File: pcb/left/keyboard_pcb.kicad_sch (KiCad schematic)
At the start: 44 parts, among them J1 TRRS, J2 Conn_01x04_Male, K0 KEYSW, K1 KEYSW, K10 KEYSW, K11 KEYSW, K12 KEYSW, K13 KEYSW, K14 KEYSW, K15 KEYSW, K2 KEYSW, K20 KEYSW, K21 KEYSW, K22 KEYSW, K23 KEYSW, K24 KEYSW, K25 KEYSW, K3 KEYSW, K30 KEYSW, K31 KEYSW, K32 KEYSW, K4 KEYSW, K5 KEYSW, U1 PCF8574, U2 Pico

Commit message: first layout left
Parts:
- C1: value C -> 10uF
- C2: value C -> 100nF
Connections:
- net I2C_Int: now also U2.22 (GPIO17); no longer U2.27 (GPIO21)
- net k00: now also U1.6 (P2); no longer U1.4 (P0)
- net k01: now also U2.15 (GPIO11); no longer U2.29 (GPIO22)
- net k03: now also U2.6 (GPIO4); no longer U2.20 (GPIO15)
- net k11: now also U2.14 (GPIO10); no longer U2.26 (GPIO20)
- net k12: now also U2.12 (GPIO9); no longer U2.24 (GPIO18)
- net k13: now also U2.11 (GPIO8); no longer U2.19 (GPIO14)
- net k14: now also U2.10 (GPIO7); no longer U2.22 (GPIO17)
- net k15: now also U2.9 (GPIO6); no longer U2.21 (GPIO16)
- net k20: now also U1.4 (P0); no longer U1.6 (P2)
- net k21: now also U2.21 (GPIO16); no longer U2.25 (GPIO19)
- net k22: now also U2.19 (GPIO14); no longer U2.9 (GPIO6)
- net k23: now also U2.16 (GPIO12); no longer U2.10 (GPIO7)
- net k24: now also U2.20 (GPIO15); no longer U2.17 (GPIO13)
- net k25: now also U2.17 (GPIO13); no longer U2.6 (GPIO4)
- no-connect marks 12 -> 11
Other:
- moved on the sheet: C1, C2, R3, R4

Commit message: Added changes on the left board
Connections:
- net SCL: no longer U2.32 (GPIO27_ADC1)
- net SDA: no longer U2.31 (GPIO26_ADC0)
- net k01: now also U2.24 (GPIO18); no longer U2.15 (GPIO11)
- net k11: now also U2.25 (GPIO19); no longer U2.14 (GPIO10)
- net k12: now also U2.32 (GPIO27_ADC1); no longer U2.12 (GPIO9)
- net k13: now also U2.31 (GPIO26_ADC0); no longer U2.11 (GPIO8)
- net k23: now also U2.26 (GPIO20); no longer U2.16 (GPIO12)
- no-connect marks 11 -> 13
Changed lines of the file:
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@@
   (junction (at 193.04 142.24) (diameter 0) (color 0 0 0 0)
   )
-  (no_connect (at 68.58 67.31))
   (no_connect (at 68.58 57.15))
-  (no_connect (at 68.58 64.77))
+  (no_connect (at 27.94 64.77))
+  (no_connect (at 27.94 54.61))
+  (no_connect (at 27.94 62.23))
+  (no_connect (at 27.94 57.15))
   (no_connect (at 53.34 82.55))
   (no_connect (at 50.8 82.55))
   (no_connect (at 48.26 82.55))
+  (no_connect (at 27.94 67.31))
   (no_connect (at 68.58 39.37))
   (no_connect (at 68.58 41.91))
   (no_connect (at 68.58 36.83))
   (no_connect (at 68.58 54.61))
-  (no_connect (at 68.58 69.85))
   (wire (pts (xy 149.86 60.96) (xy 154.94 60.96))
     (stroke (width 0) (type default) (color 0 0 0 0))
@@
     (stroke (width 0) (type default) (color 0 0 0 0))
   )
+  (polyline (pts (xy 26.67 53.34) (xy 29.21 53.34))
+    (stroke (width 0) (type default) (color 0 0 0 0))
+  )
   (wire (pts (xy 193.04 139.7) (xy 201.93 139.7))
     (stroke (width 0) (type default) (color 0 0 0 0))
@@
     (stroke (width 0) (type default) (color 0 0 0 0))
   )
+  (polyline (pts (xy 26.67 53.34) (xy 22.86 53.34))
+    (stroke (width 0) (type default) (color 0 0 0 0))
+  )
   (wire (pts (xy 248.92 124.46) (xy 248.92 120.65))
     (stroke (width 0) (type default) (color 0 0 0 0))
   )
-  (wire (pts (xy 27.94 69.85) (xy 33.02 69.85))
-    (stroke (width 0) (type default) (color 0 0 0 0))
-  )
-  (wire (pts (xy 68.58 77.47) (xy 85.09 77.47))
+  (wire (pts (xy 21.59 69.85) (xy 33.02 69.85))
     (stroke (width 0) (type default) (color 0 0 0 0))
   )
@@
     (stroke (width 0) (type default) (color 0 0 0 0))
   )
+  (polyline (pts (xy 22.86 68.58) (xy 30.48 68.58))
+    (stroke (width 0) (type default) (color 0 0 0 0))
+  )
   (wire (pts (xy 227.33 139.7) (xy 231.14 139.7))
     (stroke (width 0) (type default) (color 0 0 0 0))
@@
     (stroke (width 0) (type default) (color 0 0 0 0))
   )
+  (polyline (pts (xy 22.86 53.34) (xy 22.86 68.58))
+    (stroke (width 0) (type default) (color 0 0 0 0))
+  )
   (wire (pts (xy 271.78 78.74) (xy 271.78 76.2))
     (stroke (width 0) (type default) (color 0 0 0 0))
@@
     (stroke (width 0) (type default) (color 0 0 0 0))
   )
-  (label "k11" (at 27.94 62.23 180)
-    (effects (font (size 1.27 1.27)) (justify right bottom))
+  (label "k11" (at 68.58 67.31 0)
+    (effects (font (size 1.27 1.27)) (justify left bottom))
   )
   (label "SCL" (at 148.59 151.13 180)
@@
     (effects (font (size 1.27 1.27)) (justify left bottom))
   )
-  (label "k21" (at 85.09 77.47 0)
-    (effects (font (size 1.27 1.27)) (justify left bottom))
-  )
-  (label "k13" (at 27.94 54.61 180)
-    (effects (font (size 1.27 1.27)) (justify right bottom))
+  (label "k21" (at 68.58 77.47 0)
+    (effects (font (size 1.27 1.27)) (justify left bottom))
+  )
+  (label "k13" (at 77.47 52.07 0)
+    (effects (font (size 1.27 1.27)) (justify left bottom))
   )
   (label "k30" (at 200.66 76.2 0)
@@
     (effects (font (size 1.27 1.27)) (justify left bottom))
   )
-  (label "SDA" (at 77.47 52.07 180)
+  (label "SDA" (at 19.05 62.23 180)
     (effects (font (size 1.27 1.27)) (justify right bottom))
   )
@@
     (effects (font (size 1.27 1.27)) (justify left bottom))
   )
-  (label "k01" (at 27.94 64.77 180)
-    (effects (font (size 1.27 1.27)) (justify right bottom))
+  (label "k01" (at 68.58 69.85 0)
+    (effects (font (size 1.27 1.27)) (justify left bottom))
   )
   (label "k00" (at 124.46 30.48 0)
@@
     (effects (font (size 1.27 1.27)) (justify left bottom))
   )
-  (label "k12" (at 27.94 57.15 180)
-    (effects (font (size 1.27 1.27)) (justify right bottom))
+  (label "k12" (at 77.47 49.53 0)
+    (effects (font (size 1.27 1.27)) (justify left bottom))
   )
   (label "k30" (at 231.14 139.7 0)
@@
     (effects (font (size 1.27 1.27)) (justify left bottom))
   )
-  (label "k23" (at 27.94 67.31 180)
-    (effects (font (size 1.27 1.27)) (justify right bottom))
+  (label "k23" (at 68.58 64.77 0)
+    (effects (font (size 1.27 1.27)) (justify left bottom))
   )
   (label "k11" (at 149.86 45.72 0)
@@
     (effects (font (size 1.27 1.27)) (justify right bottom))
   )
-  (label "k25" (at 27.94 69.85 180)
+  (label "k25" (at 21.59 69.85 180)
     (effects (font (size 1.27 1.27)) (justify right bottom))
   )
@@
     (effects (font (size 1.27 1.27)) (justify left bottom))
   )
-  (label "SCL" (at 77.47 49.53 180)
+  (label "SCL" (at 19.05 64.77 180)
     (effects (font (size 1.27 1.27)) (justify right bottom))
   )
@@
     (pin "2")
   )
+  (symbol (lib_id "Graphic:Logo_Open_Hardware_Small") (at 102.87 40.64 0) (unit 1)
+    (in_bom yes) (on_board yes) (fields_autoplaced)
+    (property "Reference" "#LOGO?" (id 0) (at 102.87 33.655 0)
+      (effects (font (size 1.27 1.27)) hide)
+    )
+    (property "Value" "Logo_Open_Hardware_Small" (id 1) (at 102.87 46.355 0)
+      (effects (font (size 1.27 1.27)) hide)
+    )
+    (property "Footprint" "Symbol:KiCad-Logo2_5mm_SilkScreen" (id 2) (at 102.87 40.64 0)
+      (effects (font (size 1.27 1.27)) hide)
+    )
+    (property "Datasheet" "~" (id 3) (at 102.87 40.64 0)
+      (effects (font (size 1.27 1.27)) hide)
+    )
+  )
   (symbol (lib_id "power:GND") (at 271.78 33.02 0) (unit 1)
     (in_bom yes) (on_board yes)
@@
     (pin "1")
     (pin "2")
+  )
+  (symbol (lib_id "Graphic:Logo_Open_Hardware_Small") (at 101.6 72.39 0) (unit 1)
+    (in_bom yes) (on_board yes) (fields_autoplaced)
+    (property "Reference" "#LOGO?" (id 0) (at 101.6 65.405 0)
+      (effects (font (size 1.27 1.27)) hide)
+    )
+    (property "Value" "Logo_Open_Hardware_Small" (id 1) (at 101.6 78.105 0)
+      (effects (font (size 1.27 1.27)) hide)
+    )
+    (property "Footprint" "Symbol:OSHW-Logo_7.5x8mm_SilkScreen" (id 2) (at 101.6 72.39 0)
+      (effects (font (size 1.27 1.27)) hide)
+    )
+    (property "Datasheet" "~" (id 3) (at 101.6 72.39 0)
+      (effects (font (size 1.27 1.27)) hide)
+    )
   )
   (symbol (lib_id "power:GND") (at 33.02 72.39 270) (unit 1)
@@
   )
   (symbol_instances
+    (path "/67422531-f64c-4e79-af6e-4f9a651c4697"
+      (reference "#LOGO?") (unit 1) (value "Logo_Open_Hardware_Small") (footprint "Symbol:KiCad-Logo2_5mm_SilkScreen")
+    )
+    (path "/83460708-a7ce-4cdd-8d6e-11fedebf9607"
+      (reference "#LOGO?") (unit 1) (value "Logo_Open_Hardware_Small") (footprint "Symbol:OSHW-Logo_7.5x8mm_SilkScreen")
+    )
     (path "/f08c03f9-ecca-4ed0-9617-3646fb25a245"
       (reference "#PWR01") (unit 1) (value "VCC") (footprint "")

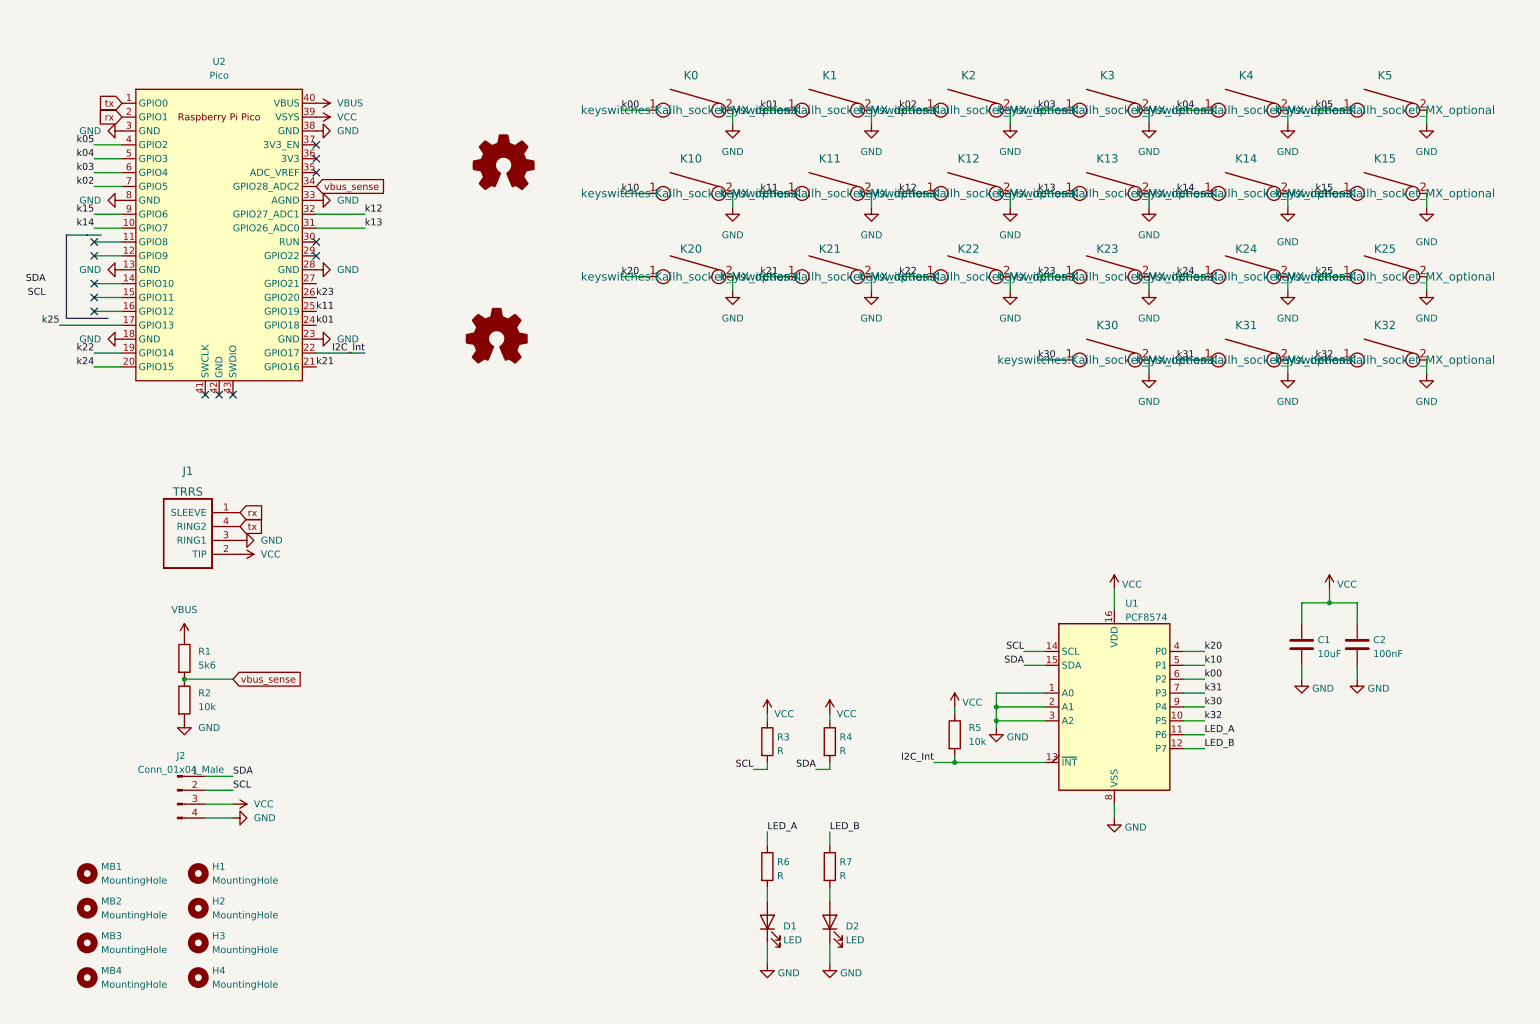
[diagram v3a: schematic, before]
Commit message: left keyboards routed
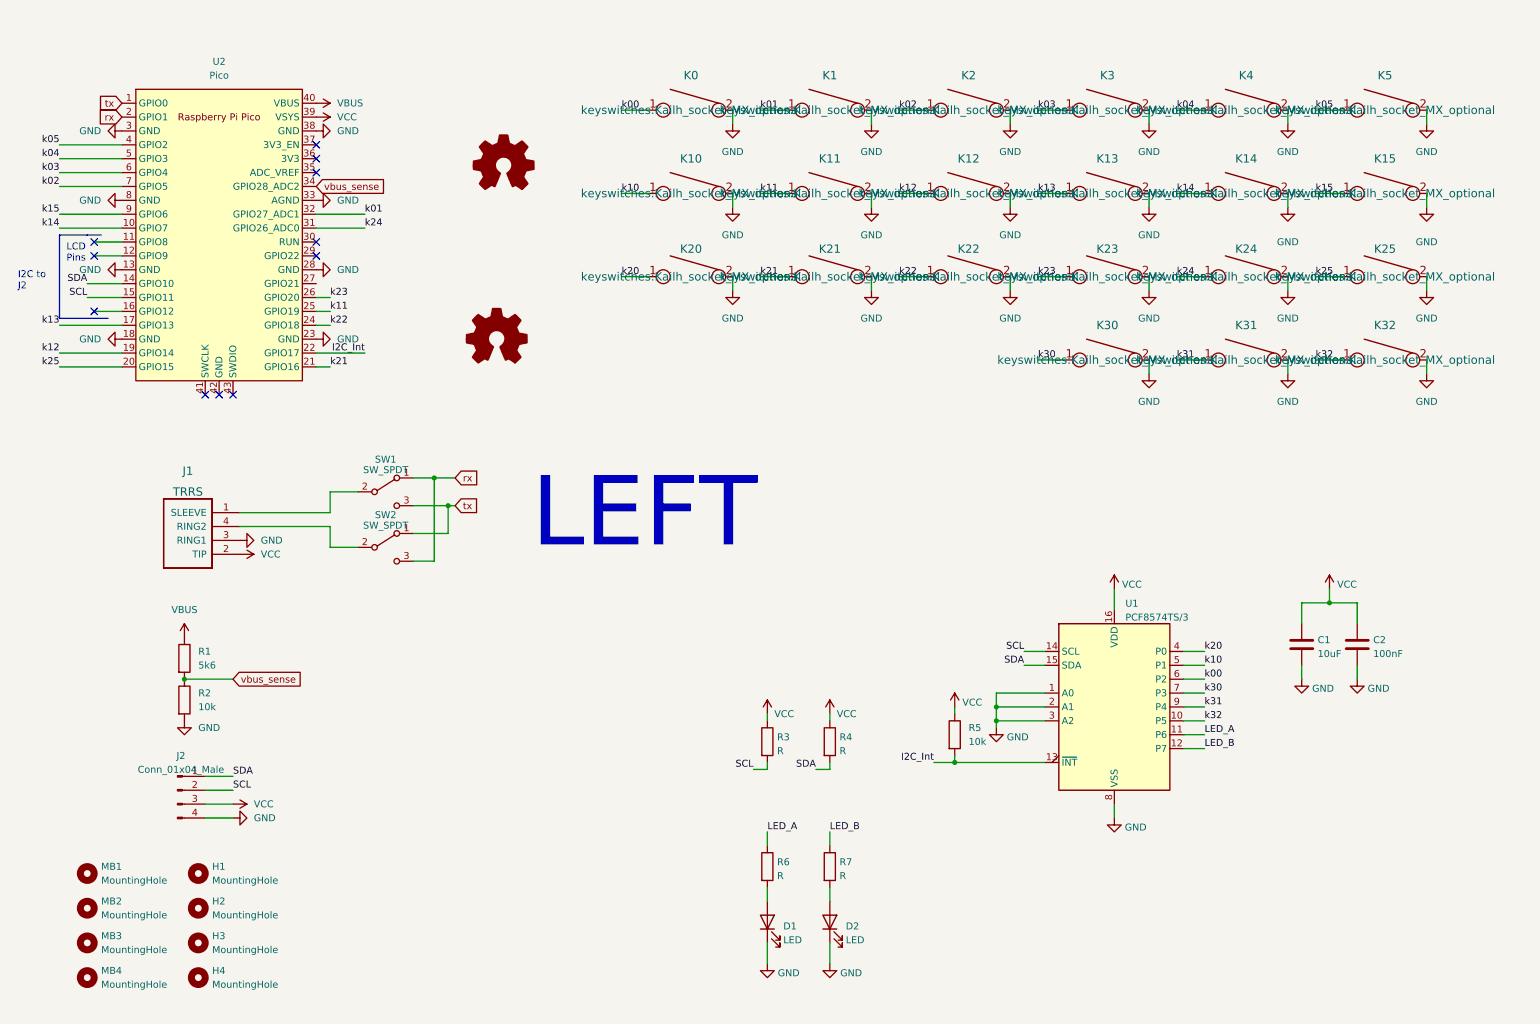
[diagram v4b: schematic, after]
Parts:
- added SW1, SW2: SW_SPDT, Jumper:SolderJumper-3_P1.3mm_Open_RoundedPad1.0x1.5mm_NumberLabels, symbol Switch:SW_SPDT
- R3, R4: footprint Resistor_SMD:R_0603_1608Metric_Pad0.98x0.95mm_HandSolder -> Resistor_SMD:R_1206_3216Metric
- U1: value PCF8574 -> PCF8574TS/3
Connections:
- net SCL: now also U2.15 (GPIO11)
- net SDA: now also U2.14 (GPIO10)
- net k01: now also U2.32 (GPIO27_ADC1); no longer U2.24 (GPIO18)
- net k12: now also U2.19 (GPIO14); no longer U2.32 (GPIO27_ADC1)
- net k13: now also U2.17 (GPIO13); no longer U2.31 (GPIO26_ADC0)
- net k22: now also U2.24 (GPIO18); no longer U2.19 (GPIO14)
- net k24: now also U2.31 (GPIO26_ADC0); no longer U2.20 (GPIO15)
- net k25: now also U2.20 (GPIO15); no longer U2.17 (GPIO13)
- net k30: now also U1.7 (P3); no longer U1.9 (P4)
- net k31: now also U1.9 (P4); no longer U1.7 (P3)
- net rx: now also SW1.1 (A), SW2.3 (C); no longer J1.1 (SLEEVE)
- net tx: now also SW1.3 (C), SW2.1 (A); no longer J1.4 (RING2)
- new net: J1.1 (SLEEVE), SW1.2 (B)
- new net: J1.4 (RING2), SW2.2 (B)
- no-connect marks 13 -> 11
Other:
- note added: "I2C to J2"
- note added: "LCD Pins"
- note added: "LEFT"
